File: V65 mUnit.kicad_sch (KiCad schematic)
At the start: 31 parts

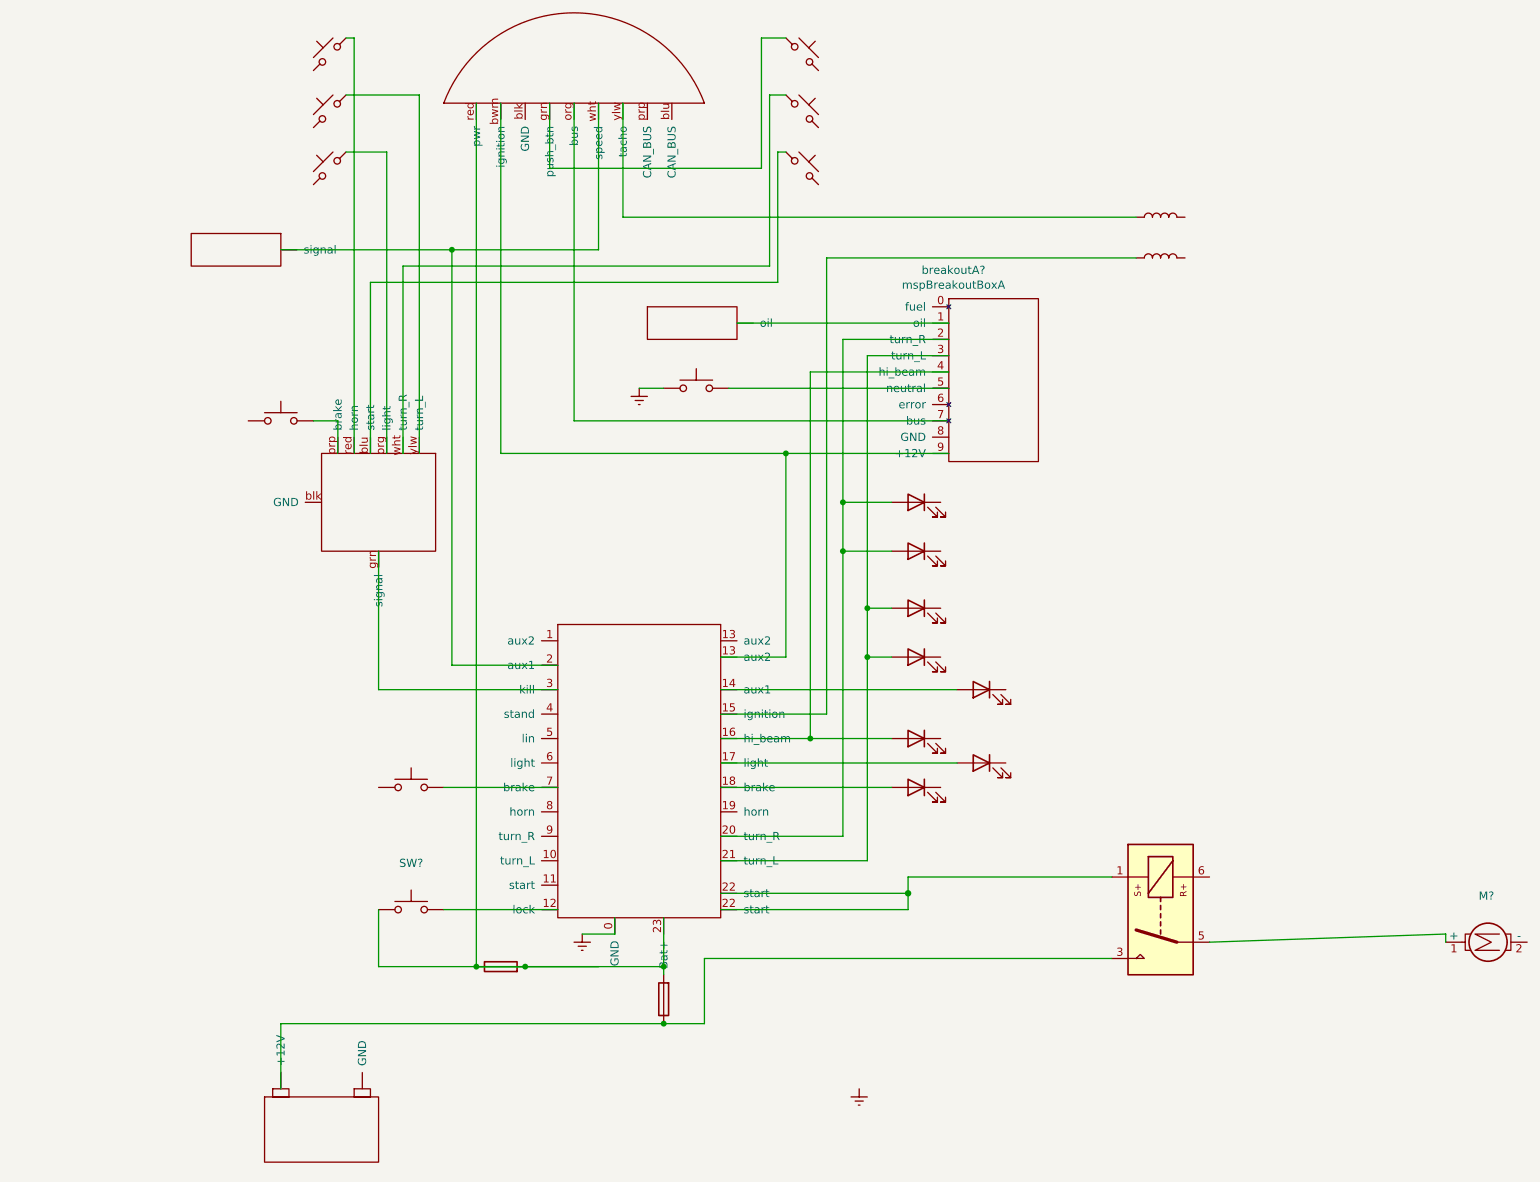
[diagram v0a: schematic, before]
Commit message: feat(ignition): added Sachse ignition
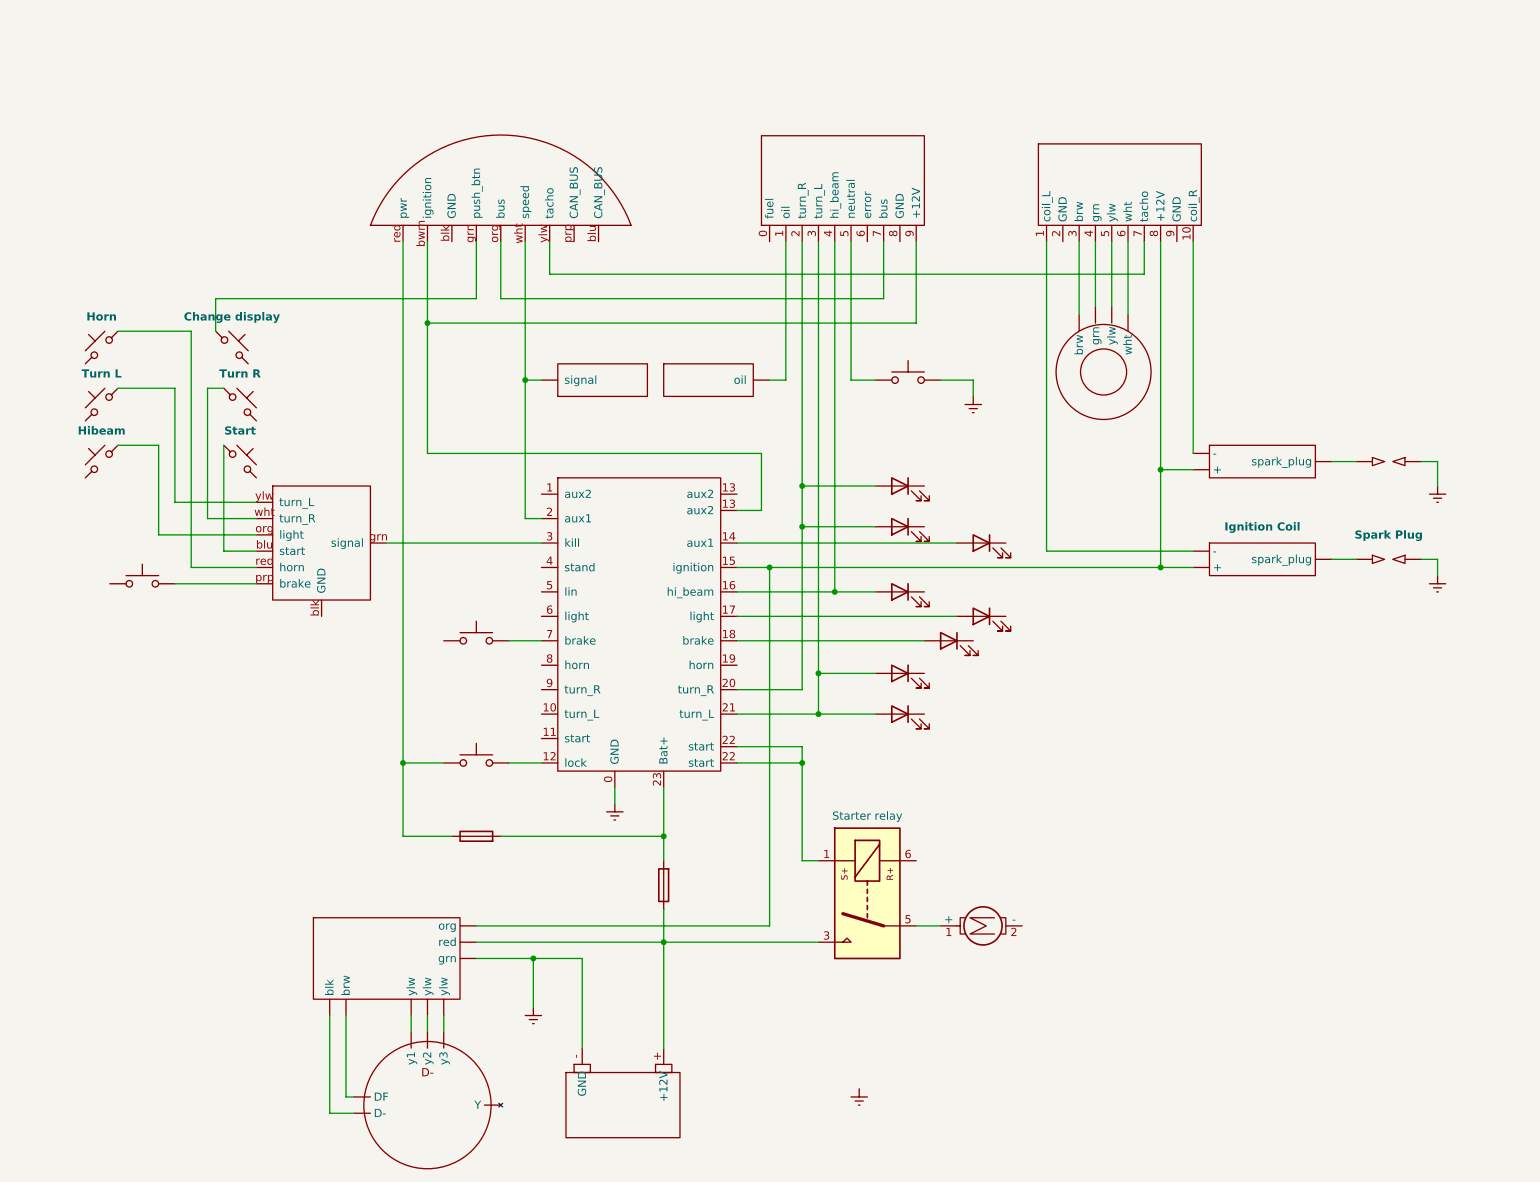
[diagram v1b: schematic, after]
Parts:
- removed L? (x2): (no value), symbol Device:L
- added E?: Spark Plug, symbol Device:SparkGap
- added E?: (no value), symbol Device:SparkGap
- added U?: (no value), symbol motorcycle:ignition_coil
- added U?: Ignition Coil, symbol motorcycle:ignition_coil
- added U?: (no value), symbol motorcycle:sachse_zdg_3.23
- added U?: (no value), symbol motorcycle:sachse pickup
- added U?: (no value), symbol motorcycle:boschStator
- added regulator_rectifier: (no value), symbol motorcycle:regulator_rectifier
- K?: value (none) -> Starter relay; footprint (none) -> Relay_THT:Relay_1P1T_NO_10x24x18.8mm_Panasonic_ADW11xxxxW_THT
- breakoutA?: value mspBreakoutBoxA -> (none)
- chg_displ: value (none) -> Change display
- hibeam: value (none) -> Hibeam
- horn: value (none) -> Horn
- start: value (none) -> Start
- turn_l: value (none) -> Turn L
- turn_r: value (none) -> Turn R
- gave numbers to parts that had none: 5
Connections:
- net Earth: now also Bat?.- (GND), SW?.2, E?.2, E?.2, regulator_rectifier. (ylw); no longer SW?.1
- net at F?.1, ignition_key.1, msp.red (pwr): no longer F?.2, F?.2, mo.unit_blue.23 (Bat+)
- net at msp.ylw (tacho): now also U?.7 (tacho)
- net at breakoutA?.1 (oil): now also Oil. (oil); no longer Oil.~ (oil)
- net at breakoutA?.5 (neutral): now also SW?.1; no longer SW?.2
- net at mo.unit_blue.15 (ignition): now also U?. (spark_plug), U?. (spark_plug), U?.8 (+12V), regulator_rectifier. (ylw)
- net at F?.1, K?.3: now also Bat?.+ (+12V), regulator_rectifier. (ylw); no longer Bat?.~ (GND)
- new net: F?.2, F?.2, mo.unit_blue.23 (Bat+)
- new net: U?. (spark_plug), U?.10 (coil_R)
- new net: E?.1, U?. (spark_plug) (x2)
- new net: U?. (spark_plug), U?.1 (coil_L)
- new net: U?. (y3), regulator_rectifier. (ylw) (x5)
- new net: U?. (ylw), U?.3 (brw)
- new net: U?. (ylw), U?.4 (grn)
- new net: U?. (ylw), U?.5 (ylw)
- new net: U?. (ylw), U?.6 (wht)

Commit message: fix(starter): Removed unneecessary relay for starter motor
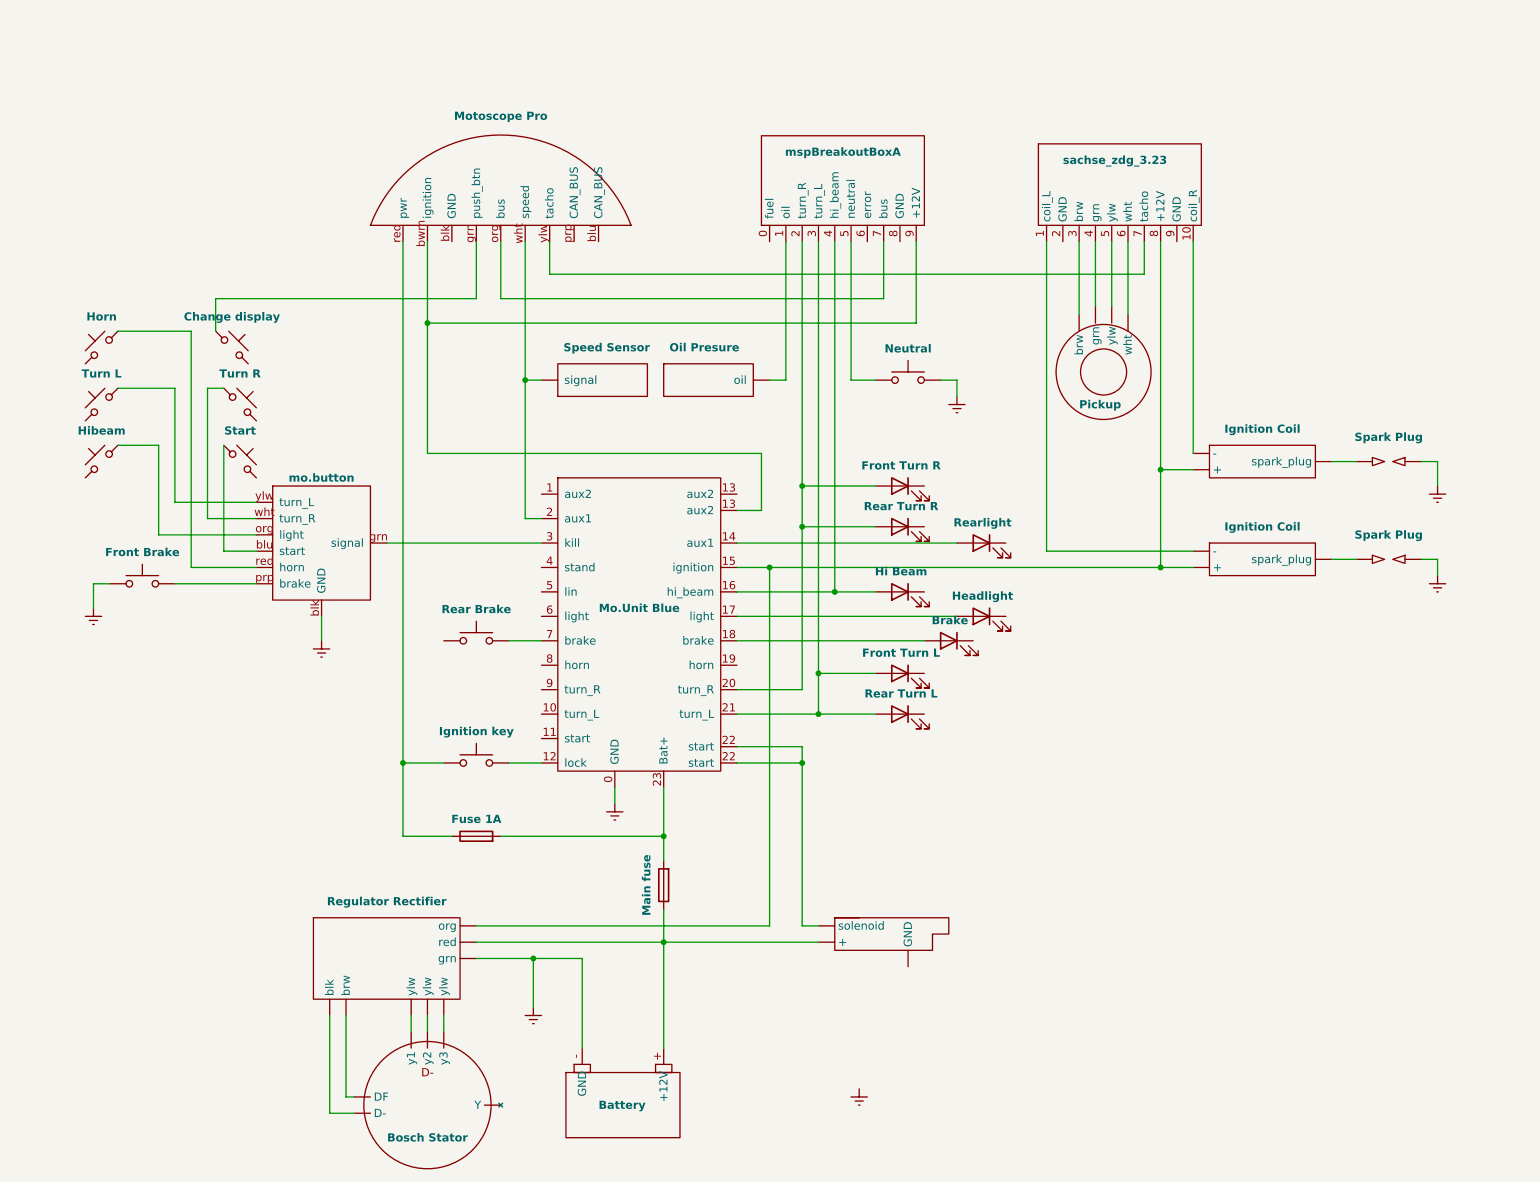
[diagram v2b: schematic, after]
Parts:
- removed K?: Starter relay, Relay_THT:Relay_1P1T_NO_10x24x18.8mm_Panasonic_ADW11xxxxW_THT, symbol Relay:ADW11
- removed starter_engine: (no value), symbol Motor:Motor_DC_ALT
- added starter_motor: (no value), symbol motorcycle:starter_motor
- B?: value (none) -> mo.button
- Bat?: value (none) -> Battery
- D?: value (none) -> Headlight
- D?: value (none) -> Hi Beam
- D?: value (none) -> Brake
- E?: value (none) -> Spark Plug
- F?: value (none) -> Fuse 1A
- F?: value (none) -> Main fuse
- Oil: value (none) -> Oil Presure
- SW?: value (none) -> Neutral
- SW?: value (none) -> Rear Brake
- U?: value (none) -> Ignition Coil
- U?: value (none) -> sachse_zdg_3.23
- U?: value (none) -> Pickup
- U?: value (none) -> Bosch Stator
- breakoutA?: value (none) -> mspBreakoutBoxA
- front_braker: value (none) -> Front Brake
- front_turn_L: value (none) -> Front Turn L
- front_turn_R: value (none) -> Front Turn R
- ignition_key: value (none) -> Ignition key
- mo.unit_blue: value (none) -> Mo.Unit Blue
- msp: value (none) -> Motoscope Pro
- rear_turn_L: value (none) -> Rear Turn L
- rear_turn_r: value (none) -> Rear Turn R
- rearlight: value (none) -> Rearlight
- regulator_rectifier: value (none) -> Regulator Rectifier
- spd?: value (none) -> Speed Sensor
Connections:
- net Earth: now also B?.blk (GND), front_braker.1
- net at mo.unit_blue.22 (start): now also starter_motor. (solenoid)
- net at Bat?.+ (+12V), F?.1, regulator_rectifier. (ylw): now also starter_motor. (solenoid)
- net at U?. (y3): no longer regulator_rectifier. (ylw)
- new net: U?. (spark_plug), U?. (spark_plug), U?.8 (+12V), mo.unit_blue.15 (ignition), regulator_rectifier. (ylw)
- new net: U?. (y3), regulator_rectifier. (ylw) (x5)
- now unconnected: U?. (y3), U?. (y3), U?. (y3), U?. (y3)

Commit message: fix(coils): Switched left and right coils from Sachse ignition after correspondence with company
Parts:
- U? (x2): value Ignition Coil -> (none)
- starter_motor: value (none) -> Starter Motor
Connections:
- net Earth: now also U?.9 (GND)
- net at U?. (y3): no longer regulator_rectifier. (ylw)
- new net: U?. (spark_plug), U?. (spark_plug), U?.8 (+12V), mo.unit_blue.15 (ignition), regulator_rectifier. (ylw)
- new net: U?. (y3), regulator_rectifier. (ylw) (x5)
- now unconnected: U?. (y3), U?. (y3), U?. (y3), U?. (y3)
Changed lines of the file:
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@@
     (stroke (width 0) (type default) (color 0 132 0 1))
+  )
+  (wire (pts (xy 228.6 50.8) (xy 228.6 53.34))
+    (stroke (width 0) (type default) (color 0 0 0 0))
   )
   (wire (pts (xy 160.02 120.65) (xy 170.18 120.65))
@@
       (effects (font (size 1.27 1.27)) hide)
     )
-    (property "Value" "Ignition Coil" (id 1) (at 241.935 80.01 0)
+    (property "Value" "" (id 1) (at 241.935 80.01 0)
       (effects (font (size 1.27 1.27) bold))
     )
@@
       (effects (font (size 1.27 1.27)) hide)
     )
-    (property "Value" "Ignition Coil" (id 1) (at 241.935 95.25 0)
+    (property "Value" "" (id 1) (at 241.935 95.25 0)
       (effects (font (size 1.27 1.27) bold))
     )
@@
       (effects (font (size 1.27 1.27)) (justify left) hide)
     )
-    (property "Value" "" (id 1) (at 177.8 154.94 0)
+    (property "Value" "Starter Motor" (id 1) (at 177.8 154.94 0)
       (effects (font (size 1.27 1.27) bold) (justify left))
     )
@@
     (pin "")
   )
+  (symbol (lib_id "power:Earth") (at 228.6 53.34 0) (unit 1)
+    (in_bom yes) (on_board yes) (fields_autoplaced)
+    (property "Reference" "#PWR?" (id 0) (at 228.6 59.69 0)
+      (effects (font (size 1.27 1.27)) hide)
+    )
+    (property "Value" "Earth" (id 1) (at 228.6 57.15 0)
+      (effects (font (size 1.27 1.27)) hide)
+    )
+    (property "Footprint" "" (id 2) (at 228.6 53.34 0)
+      (effects (font (size 1.27 1.27)) hide)
+    )
+    (property "Datasheet" "~" (id 3) (at 228.6 53.34 0)
+      (effects (font (size 1.27 1.27)) hide)
+    )
+    (pin "1")
+  )
   (sheet_instances
     (path "/" (page "1"))
@@
       (reference "#PWR?") (unit 1) (value "Earth") (footprint "")
     )
+    (path "/ff9a2c4e-2b56-4901-8019-7f4eeb4f7312"
+      (reference "#PWR?") (unit 1) (value "Earth") (footprint "")
+    )
     (path "/00000000-0000-0000-0000-00005fbafd7d"
       (reference "B?") (unit 1) (value "mo.button") (footprint "")
@@
     )
     (path "/23789c5e-f2d5-448b-919e-205074d0efcc"
-      (reference "U?") (unit 1) (value "Ignition Coil") (footprint "")
+      (reference "U?") (unit 1) (value "Left Ignition Coil") (footprint "")
     )
     (path "/55cd0c33-b843-4337-b4af-5848004f6995"
-      (reference "U?") (unit 1) (value "Ignition Coil") (footprint "")
+      (reference "U?") (unit 1) (value "Right Ignition Coil") (footprint "")
     )
     (path "/cfb340bc-8887-49ee-a5d4-7bfe9d7573b9"

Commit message: feat(usb): added USB charger
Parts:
- added USB?: USB Charger, symbol motorcycle:usb_charger
- Oil: value Oil Presure -> Oil Pressure
- U?: value (none) -> Left Ignition Coil
- U?: value (none) -> Right Ignition Coil
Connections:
- net Earth: now also SW?.1, U?.2 (GND), breakoutA?.8 (GND), starter_motor. (solenoid), USB?. (GND)
- net at msp.wht (speed), spd?.~ (signal): now also mo.unit_blue.1 (aux2); no longer mo.unit_blue.2 (aux1)
- net at mo.unit_blue.13 (aux2): now also USB?. (GND)
- net at U?. (y3): no longer regulator_rectifier. (ylw)
- new net: U?. (spark_plug), U?. (spark_plug), U?.8 (+12V), mo.unit_blue.15 (ignition), regulator_rectifier. (ylw)
- new net: U?. (y3), regulator_rectifier. (ylw) (x5)
- now unconnected: U?. (y3), U?. (y3), U?. (y3), U?. (y3)

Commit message: chore: cleanup
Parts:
- gave numbers to parts that had none: 19
- renumbered Oil to Oil1, chg_displ to chg_displ1, front_braker to front_braker1, front_turn_L to front_turn_L1, front_turn_R to front_turn_R1, hibeam to hibeam1, horn to horn1, ignition_key to ignition_key1, mo.unit_blue to mo.unit_blue1, msp to msp1, rear_turn_L to rear_turn_L1, rear_turn_r to rear_turn_r1, rearlight to rearlight1, regulator_rectifier to regulator_rectifier1, start to start1, starter_motor to starter_motor1, turn_l to turn_l1, turn_r to turn_r1
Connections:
- net at U1. (y3): no longer regulator_rectifier1. (ylw)
- new net: breakoutA1.9 (+12V), mo.unit_blue1.13 (aux2), msp1.brn (ignition)
- new net: U3.8 (+12V), U4. (spark_plug), U5. (spark_plug), mo.unit_blue1.15 (ignition), regulator_rectifier1. (ylw)
- new net: U1. (y3), regulator_rectifier1. (ylw) (x5)
- now unconnected: U1. (y3), U1. (y3), U1. (y3), U1. (y3)
